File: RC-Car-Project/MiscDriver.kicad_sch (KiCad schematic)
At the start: 6 parts, among them Q3 2N7002E, Q4 2N7002E

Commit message: Finished Buck
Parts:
- R1, R16, R19, R20: footprint (none) -> Resistor_SMD:R_0201_0603Metric
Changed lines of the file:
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@@
 			)
 		)
-		(property "Footprint" ""
+		(property "Footprint" "Resistor_SMD:R_0201_0603Metric"
 			(at 120.65 67.818 90)
 			(effects
@@
 			)
 		)
-		(property "Footprint" ""
+		(property "Footprint" "Resistor_SMD:R_0201_0603Metric"
 			(at 128.778 69.85 90)
 			(effects
@@
 			)
 		)
-		(property "Footprint" ""
+		(property "Footprint" "Resistor_SMD:R_0201_0603Metric"
 			(at 128.778 110.49 90)
 			(effects
@@
 			)
 		)
-		(property "Footprint" ""
+		(property "Footprint" "Resistor_SMD:R_0201_0603Metric"
 			(at 120.65 108.458 90)
 			(effects

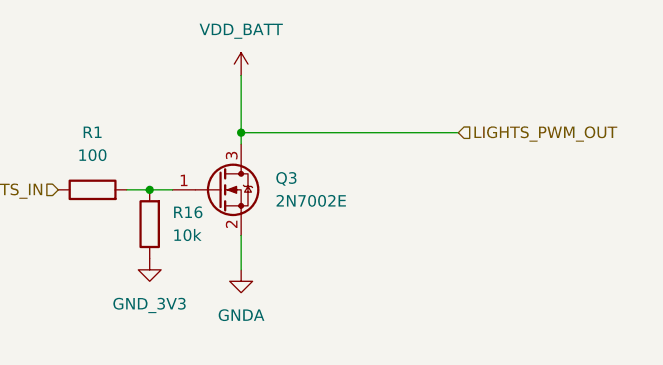
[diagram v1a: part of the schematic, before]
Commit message: Added LED Driver
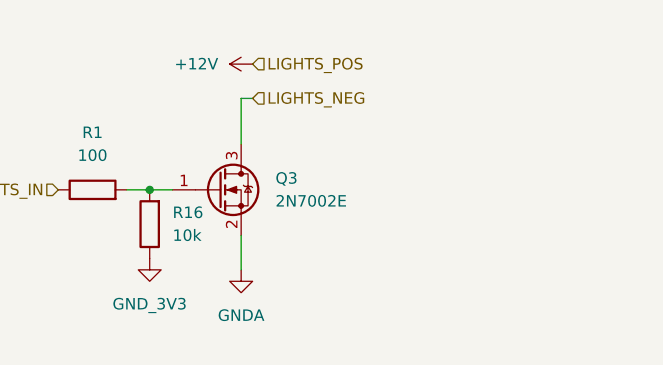
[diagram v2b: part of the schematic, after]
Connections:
- net VDD_BATT: no longer Q3.3 (D)
- new net LIGHTS_NEG: Q3.3 (D)
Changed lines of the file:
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@@
-	)
-	(junction
-		(at 137.16 59.69)
-		(diameter 0)
-		(color 0 0 0 0)
 	)
 	(junction
@@
 	(wire
 		(pts
+			(xy 137.16 55.88) (xy 138.43 55.88)
+		)
+		(stroke
+			(width 0)
+			(type default)
+		)
+	)
+	(wire
+		(pts
 			(xy 127 106.68) (xy 129.54 106.68)
 		)
@@
 	(wire
 		(pts
-			(xy 161.29 59.69) (xy 137.16 59.69)
-		)
-		(stroke
-			(width 0)
-			(type default)
-		)
-	)
-	(wire
-		(pts
-			(xy 137.16 59.69) (xy 137.16 60.96)
+			(xy 137.16 55.88) (xy 137.16 60.96)
 		)
 		(stroke
@@
 		(pts
 			(xy 124.46 106.68) (xy 127 106.68)
-		)
-		(stroke
-			(width 0)
-			(type default)
-		)
-	)
-	(wire
-		(pts
-			(xy 137.16 53.34) (xy 137.16 59.69)
 		)
 		(stroke
@@
 		)
 	)
-	(hierarchical_label "LIGHTS_PWM_OUT"
+	(hierarchical_label "LIGHTS_NEG"
 		(shape input)
-		(at 161.29 59.69 0)
+		(at 138.43 55.88 0)
+		(fields_autoplaced yes)
+		(effects
+			(font
+				(size 1.27 1.27)
+			)
+			(justify left)
+		)
+	)
+	(hierarchical_label "LIGHTS_POS"
+		(shape input)
+		(at 138.43 52.07 0)
 		(fields_autoplaced yes)
 		(effects
@@
 	)
 	(symbol
-		(lib_id "power:+3V3")
-		(at 137.16 53.34 0)
-		(unit 1)
-		(exclude_from_sim no)
-		(in_bom yes)
-		(on_board yes)
-		(dnp no)
-		(fields_autoplaced yes)
-		(property "Reference" "#PWR0103"
-			(at 137.16 57.15 0)
-			(effects
-				(font
-					(size 1.27 1.27)
-				)
-				(hide yes)
-			)
-		)
-		(property "Value" "VDD_BATT"
-			(at 137.16 48.26 0)
-			(effects
-				(font
-					(size 1.27 1.27)
-				)
-			)
-		)
-		(property "Footprint" ""
-			(at 137.16 53.34 0)
-			(effects
-				(font
-					(size 1.27 1.27)
-				)
-				(hide yes)
-			)
-		)
-		(property "Datasheet" ""
-			(at 137.16 53.34 0)
-			(effects
-				(font
-					(size 1.27 1.27)
-				)
-				(hide yes)
-			)
-		)
-		(property "Description" "Power symbol creates a global label with name \"+3V3\""
-			(at 137.16 53.34 0)
-			(effects
-				(font
-					(size 1.27 1.27)
-				)
-				(hide yes)
-			)
-		)
-		(pin "1"
-		)
-		(instances
-			(project "RC-Car-Project"
-				(path "/ba870fd1-751d-4755-8e1a-1ea86ca9e2f6/6cd00c1a-14cd-4705-8fa1-76b1c50e2463"
-					(reference "#PWR0103")
-					(unit 1)
-				)
-			)
-		)
-	)
-	(symbol
 		(lib_id "power:GNDA")
 		(at 137.16 115.57 0)
@@
 					(unit 1)
 				)
+			)
+		)
+	)
+	(symbol
+		(lib_id "power:+3V3")
+		(at 138.43 52.07 90)
+		(unit 1)
+		(exclude_from_sim no)
+		(in_bom yes)
+		(on_board yes)
+		(dnp no)
+		(fields_autoplaced yes)
+		(property "Reference" "#PWR0119"
+			(at 142.24 52.07 0)
+			(effects
+				(font
+					(size 1.27 1.27)
+				)
+				(hide yes)
+			)
+		)
+		(property "Value" "+12V"
+			(at 134.62 52.0699 90)
+			(effects
+				(font
+					(size 1.27 1.27)
+				)
+				(justify left)
+			)
+		)
+		(property "Footprint" ""
+			(at 138.43 52.07 0)
+			(effects
+				(font
+					(size 1.27 1.27)
+				)
+				(hide yes)
+			)
+		)
+		(property "Datasheet" ""
+			(at 138.43 52.07 0)
+			(effects
+				(font
+					(size 1.27 1.27)
+				)
+				(hide yes)
+			)
+		)
+		(property "Description" "Power symbol creates a global label with name \"+3V3\""
+			(at 138.43 52.07 0)
+			(effects
+				(font
+					(size 1.27 1.27)
+				)
+				(hide yes)
+			)
+		)
+		(pin "1"
+		)
+		(instances
+			(project "RC-Car-Project"
+				(path "/ba870fd1-751d-4755-8e1a-1ea86ca9e2f6/6cd00c1a-14cd-4705-8fa1-76b1c50e2463"
+					(reference "#PWR0119")
+					(unit 1)
+				)

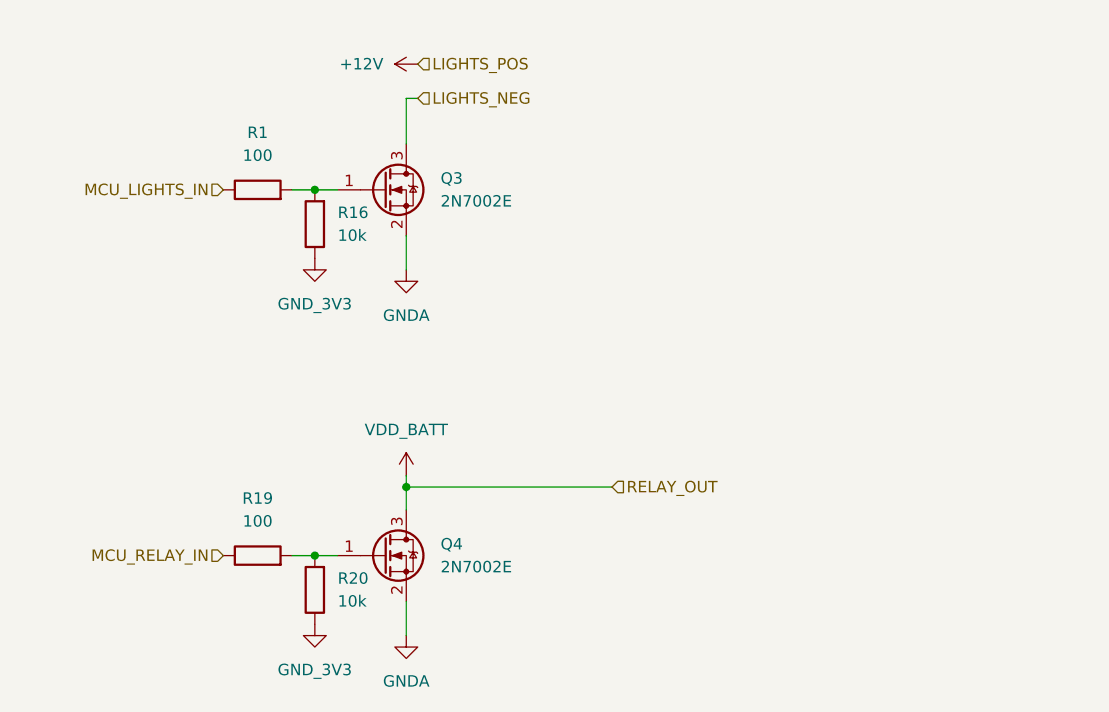
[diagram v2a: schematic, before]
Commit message: Fixed LED Drivers
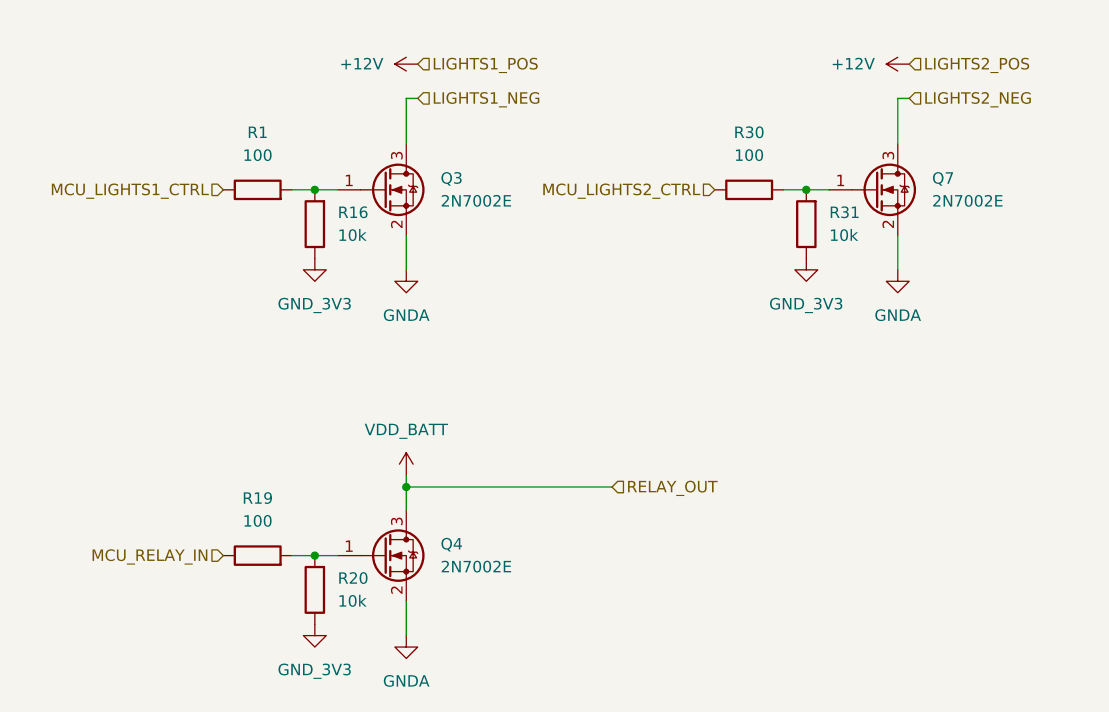
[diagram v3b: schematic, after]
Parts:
- added Q7: 2N7002E, Package_TO_SOT_SMD:SOT-23, symbol Transistor_FET:2N7002E
- added R30: 100, Resistor_SMD:R_0201_0603Metric, symbol Device:R
- added R31: 10k, Resistor_SMD:R_0201_0603Metric, symbol Device:R
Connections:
- net GNDA: now also Q7.2 (S)
- net GND_3V3: now also R31.1
- net LIGHTS_NEG renamed LIGHTS1_NEG
- net MCU_LIGHTS_IN renamed MCU_LIGHTS1_CTRL
- new net: Q7.1 (G), R30.2, R31.2
- new net LIGHTS2_NEG: Q7.3 (D)
- new net MCU_LIGHTS2_CTRL: R30.1

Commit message: Fixed Drivers
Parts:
- removed Q4: 2N7002E, Package_TO_SOT_SMD:SOT-23, symbol Transistor_FET:2N7002E
- removed R19: 100, Resistor_SMD:R_0201_0603Metric, symbol Device:R
- removed R20: 10k, Resistor_SMD:R_0201_0603Metric, symbol Device:R
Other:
- moved on the sheet: Q7, R30, R31

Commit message: Fixed Annotations
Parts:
- R30: renamed from R1; footprint Resistor_SMD:R_0201_0603Metric -> Resistor_SMD:R_0603_1608Metric
- R31: renamed from R30; footprint Resistor_SMD:R_0201_0603Metric -> Resistor_SMD:R_0603_1608Metric
- R32: renamed from R16; footprint Resistor_SMD:R_0201_0603Metric -> Resistor_SMD:R_0603_1608Metric
- R33: renamed from R31; footprint Resistor_SMD:R_0201_0603Metric -> Resistor_SMD:R_0603_1608Metric
- renumbered Q3 to Q5, Q7 to Q6
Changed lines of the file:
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@@
 		(dnp no)
 		(fields_autoplaced yes)
-		(property "Reference" "#PWR090"
+		(property "Reference" "#PWR0123"
 			(at 127 80.01 0)
 			(effects
@@
 			(project "RC-Car-Project"
 				(path "/ba870fd1-751d-4755-8e1a-1ea86ca9e2f6/6cd00c1a-14cd-4705-8fa1-76b1c50e2463"
-					(reference "#PWR090")
+					(reference "#PWR0123")
 					(unit 1)
 				)
@@
 		(dnp no)
 		(fields_autoplaced yes)
-		(property "Reference" "#PWR088"
+		(property "Reference" "#PWR0125"
 			(at 137.16 81.28 0)
 			(effects
@@
 			(project "RC-Car-Project"
 				(path "/ba870fd1-751d-4755-8e1a-1ea86ca9e2f6/6cd00c1a-14cd-4705-8fa1-76b1c50e2463"
-					(reference "#PWR088")
+					(reference "#PWR0125")
 					(unit 1)
 				)
@@
 		(dnp no)
 		(fields_autoplaced yes)
-		(property "Reference" "R1"
+		(property "Reference" "R30"
 			(at 120.65 59.69 90)
 			(effects
@@
 			)
 		)
-		(property "Footprint" "Resistor_SMD:R_0201_0603Metric"
+		(property "Footprint" "Resistor_SMD:R_0603_1608Metric"
 			(at 120.65 67.818 90)
 			(effects
@@
 			(project ""
 				(path "/ba870fd1-751d-4755-8e1a-1ea86ca9e2f6/6cd00c1a-14cd-4705-8fa1-76b1c50e2463"
-					(reference "R1")
+					(reference "R30")
 					(unit 1)
 				)
@@
 		(dnp no)
 		(fields_autoplaced yes)
-		(property "Reference" "R31"
+		(property "Reference" "R33"
 			(at 129.54 101.5999 0)
 			(effects
@@
 			)
 		)
-		(property "Footprint" "Resistor_SMD:R_0201_0603Metric"
+		(property "Footprint" "Resistor_SMD:R_0603_1608Metric"
 			(at 128.778 102.87 90)
 			(effects
@@
 			(project "RC-Car-Project"
 				(path "/ba870fd1-751d-4755-8e1a-1ea86ca9e2f6/6cd00c1a-14cd-4705-8fa1-76b1c50e2463"
-					(reference "R31")
+					(reference "R33")
 					(unit 1)
 				)
@@
 		(dnp no)
 		(fields_autoplaced yes)
-		(property "Reference" "R30"
+		(property "Reference" "R31"
 			(at 120.65 92.71 90)
 			(effects
@@
 			)
 		)
-		(property "Footprint" "Resistor_SMD:R_0201_0603Metric"
+		(property "Footprint" "Resistor_SMD:R_0603_1608Metric"
 			(at 120.65 100.838 90)
 			(effects
@@
 			(project "RC-Car-Project"
 				(path "/ba870fd1-751d-4755-8e1a-1ea86ca9e2f6/6cd00c1a-14cd-4705-8fa1-76b1c50e2463"
-					(reference "R30")
+					(reference "R31")
 					(unit 1)
 				)
@@
 		(dnp no)
 		(fields_autoplaced yes)
-		(property "Reference" "Q7"
+		(property "Reference" "Q6"
 			(at 140.97 97.7899 0)
 			(effects
@@
 			(project "RC-Car-Project"
 				(path "/ba870fd1-751d-4755-8e1a-1ea86ca9e2f6/6cd00c1a-14cd-4705-8fa1-76b1c50e2463"
-					(reference "Q7")
+					(reference "Q6")
 					(unit 1)
 				)
@@
 		(dnp no)
 		(fields_autoplaced yes)
-		(property "Reference" "#PWR0123"
+		(property "Reference" "#PWR0126"
 			(at 137.16 114.3 0)
 			(effects
@@
 			(project "RC-Car-Project"
 				(path "/ba870fd1-751d-4755-8e1a-1ea86ca9e2f6/6cd00c1a-14cd-4705-8fa1-76b1c50e2463"
-					(reference "#PWR0123")
+					(reference "#PWR0126")
 					(unit 1)
 				)
@@
 		(dnp no)
 		(fields_autoplaced yes)
-		(property "Reference" "#PWR0119"
+		(property "Reference" "#PWR0127"
 			(at 142.24 52.07 0)
 			(effects
@@
 			(project "RC-Car-Project"
 				(path "/ba870fd1-751d-4755-8e1a-1ea86ca9e2f6/6cd00c1a-14cd-4705-8fa1-76b1c50e2463"
-					(reference "#PWR0119")
+					(reference "#PWR0127")
 					(unit 1)
 				)
@@
 		(dnp no)
 		(fields_autoplaced yes)
-		(property "Reference" "R16"
+		(property "Reference" "R32"
 			(at 129.54 68.5799 0)
 			(effects
@@
 			)
 		)
-		(property "Footprint" "Resistor_SMD:R_0201_0603Metric"
+		(property "Footprint" "Resistor_SMD:R_0603_1608Metric"
 			(at 128.778 69.85 90)
 			(effects
@@
 			(project "RC-Car-Project"
 				(path "/ba870fd1-751d-4755-8e1a-1ea86ca9e2f6/6cd00c1a-14cd-4705-8fa1-76b1c50e2463"
-					(reference "R16")
+					(reference "R32")
 					(unit 1)
 				)
@@
 		(dnp no)
 		(fields_autoplaced yes)
-		(property "Reference" "Q3"
+		(property "Reference" "Q5"
 			(at 140.97 64.7699 0)
 			(effects
@@
 			(project ""
 				(path "/ba870fd1-751d-4755-8e1a-1ea86ca9e2f6/6cd00c1a-14cd-4705-8fa1-76b1c50e2463"
-					(reference "Q3")
+					(reference "Q5")
 					(unit 1)
 				)
@@
 		(dnp no)
 		(fields_autoplaced yes)
-		(property "Reference" "#PWR0103"
+		(property "Reference" "#PWR0124"
 			(at 127 113.03 0)
 			(effects
@@
 			(project "RC-Car-Project"
 				(path "/ba870fd1-751d-4755-8e1a-1ea86ca9e2f6/6cd00c1a-14cd-4705-8fa1-76b1c50e2463"
-					(reference "#PWR0103")
+					(reference "#PWR0124")
 					(unit 1)
 				)
@@
 		(dnp no)
 		(fields_autoplaced yes)
-		(property "Reference" "#PWR0124"
+		(property "Reference" "#PWR0128"
 			(at 142.24 85.09 0)
 			(effects
@@
 			(project "RC-Car-Project"
 				(path "/ba870fd1-751d-4755-8e1a-1ea86ca9e2f6/6cd00c1a-14cd-4705-8fa1-76b1c50e2463"
-					(reference "#PWR0124")
-					(unit 1)
-				)
+					(reference "#PWR0128")
+					(unit 1)
+				)

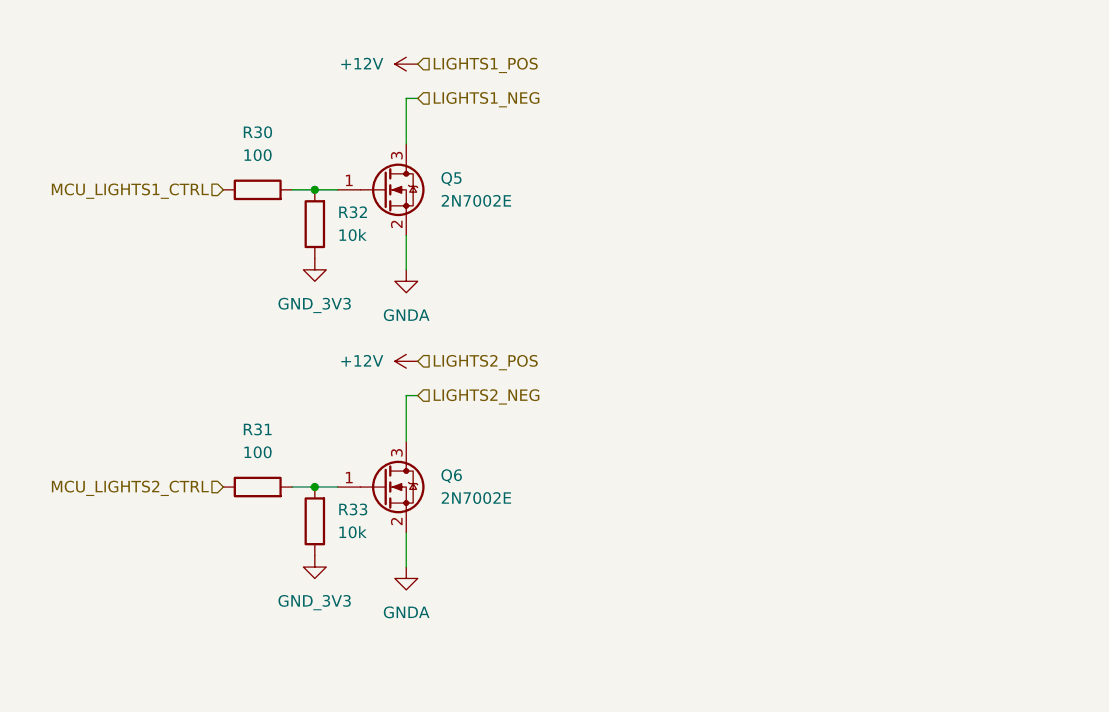
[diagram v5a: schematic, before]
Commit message: Finished prelim. Car and added screw holes
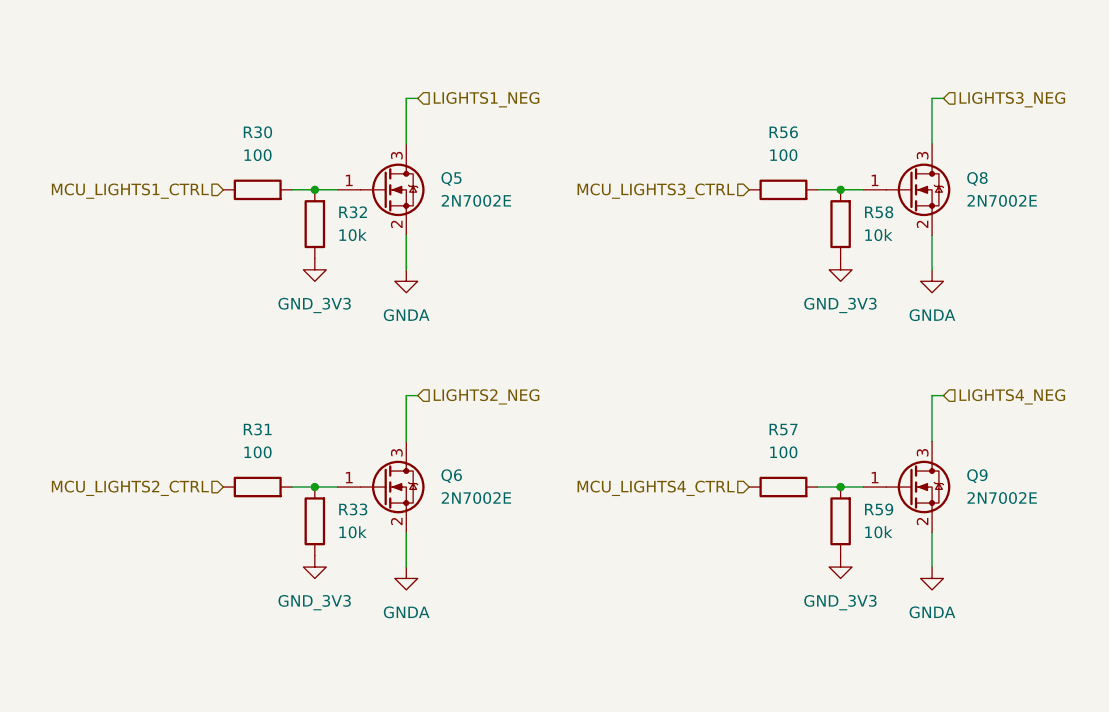
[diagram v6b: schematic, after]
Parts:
- added Q8, Q9: 2N7002E, Package_TO_SOT_SMD:SOT-23, symbol Transistor_FET:2N7002E
- added R56, R57: 100, Resistor_SMD:R_0603_1608Metric, symbol Device:R
- added R58, R59: 10k, Resistor_SMD:R_0603_1608Metric, symbol Device:R
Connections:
- net GNDA: now also Q8.2 (S), Q9.2 (S)
- net GND_3V3: now also R58.1, R59.1
- new net: Q9.1 (G), R57.2, R59.2
- new net: Q8.1 (G), R56.2, R58.2
- new net LIGHTS3_NEG: Q8.3 (D)
- new net LIGHTS4_NEG: Q9.3 (D)
- new net MCU_LIGHTS3_CTRL: R56.1
- new net MCU_LIGHTS4_CTRL: R57.1

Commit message: Fixed Resistors
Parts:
- Q5, Q6, Q8, Q9: value 2N7002E -> PMF250XNE
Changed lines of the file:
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@@
 			)
 		)
-		(property "Value" "2N7002E"
+		(property "Value" "PMF250XNE"
 			(at 140.97 100.3299 0)
 			(effects
@@
 			)
 		)
-		(property "Datasheet" "http://www.diodes.com/assets/Datasheets/ds30376.pdf"
+		(property "Datasheet" "https://assets.nexperia.com/documents/data-sheet/PMF250XNE.pdf"
 			(at 139.7 102.87 0)
 			(effects
@@
 			)
 		)
-		(property "Value" "2N7002E"
+		(property "Value" "PMF250XNE"
 			(at 199.39 100.3299 0)
 			(effects
@@
 			)
 		)
-		(property "Datasheet" "http://www.diodes.com/assets/Datasheets/ds30376.pdf"
+		(property "Datasheet" "https://assets.nexperia.com/documents/data-sheet/PMF250XNE.pdf"
 			(at 198.12 102.87 0)
 			(effects
@@
 			)
 		)
-		(property "Value" "2N7002E"
+		(property "Value" "PMF250XNE"
 			(at 140.97 67.3099 0)
 			(effects
@@
 			)
 		)
-		(property "Datasheet" "http://www.diodes.com/assets/Datasheets/ds30376.pdf"
+		(property "Datasheet" "https://assets.nexperia.com/documents/data-sheet/PMF250XNE.pdf"
 			(at 139.7 69.85 0)
 			(effects
@@
 			)
 		)
-		(property "Value" "2N7002E"
+		(property "Value" "PMF250XNE"
 			(at 199.39 67.3099 0)
 			(effects
@@
 			)
 		)
-		(property "Datasheet" "http://www.diodes.com/assets/Datasheets/ds30376.pdf"
+		(property "Datasheet" "https://assets.nexperia.com/documents/data-sheet/PMF250XNE.pdf"
 			(at 198.12 69.85 0)
 			(effects
